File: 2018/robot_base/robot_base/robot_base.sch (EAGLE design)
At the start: 38 parts

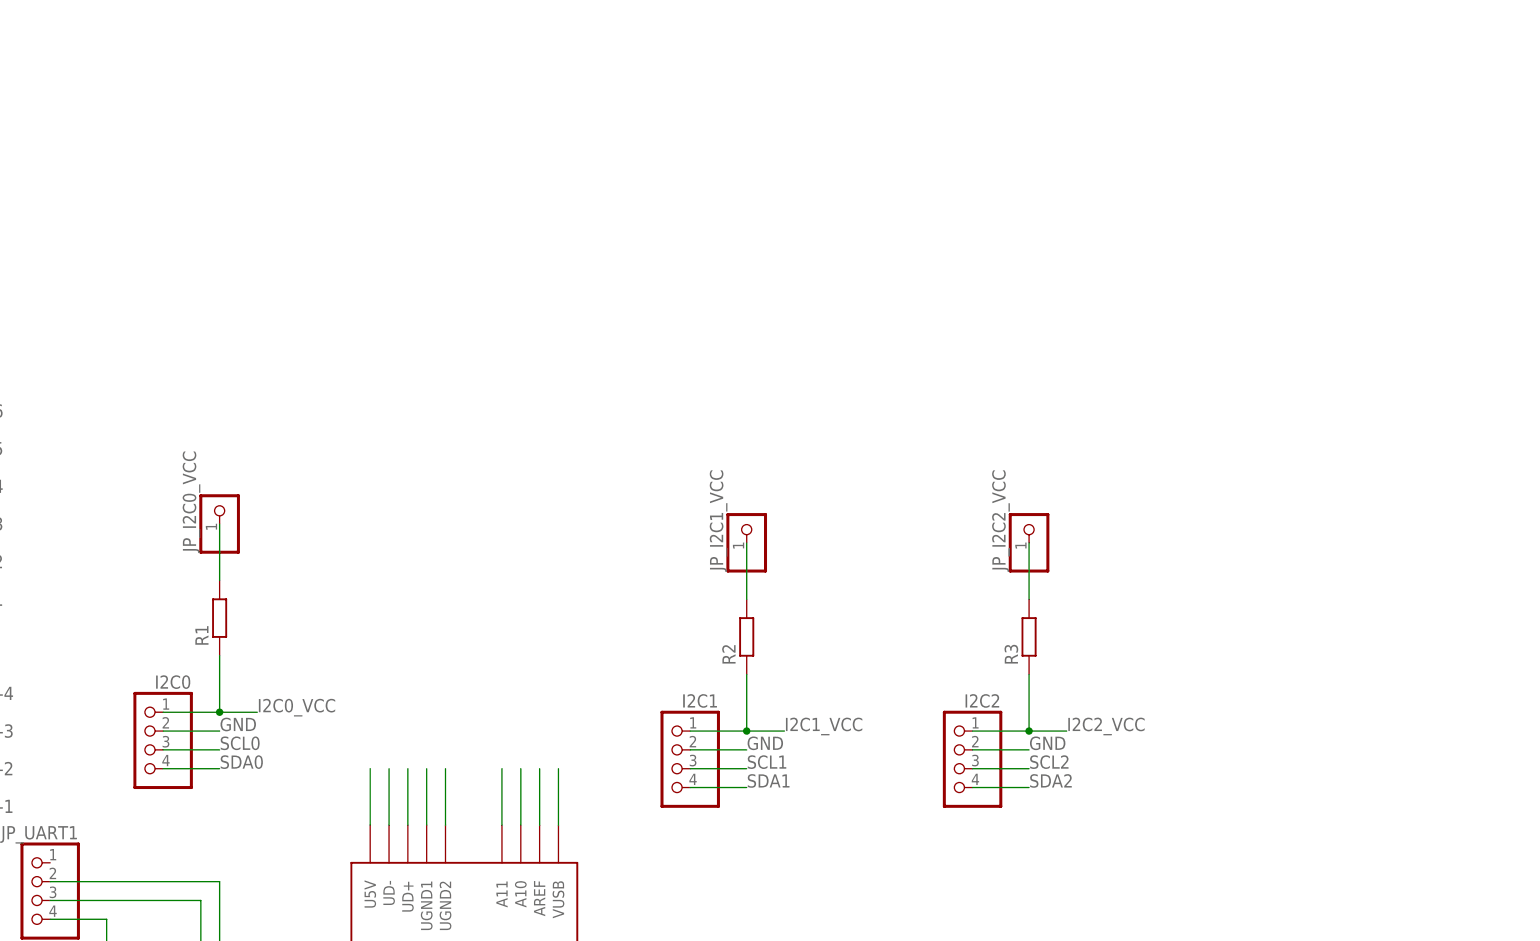
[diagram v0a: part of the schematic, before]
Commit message: Changed I2C Pull-Up resistor selector to match I2C specifications
Note: I2C Resistors doesn't have any value yet. Assessment of line
capacitance is in progress...
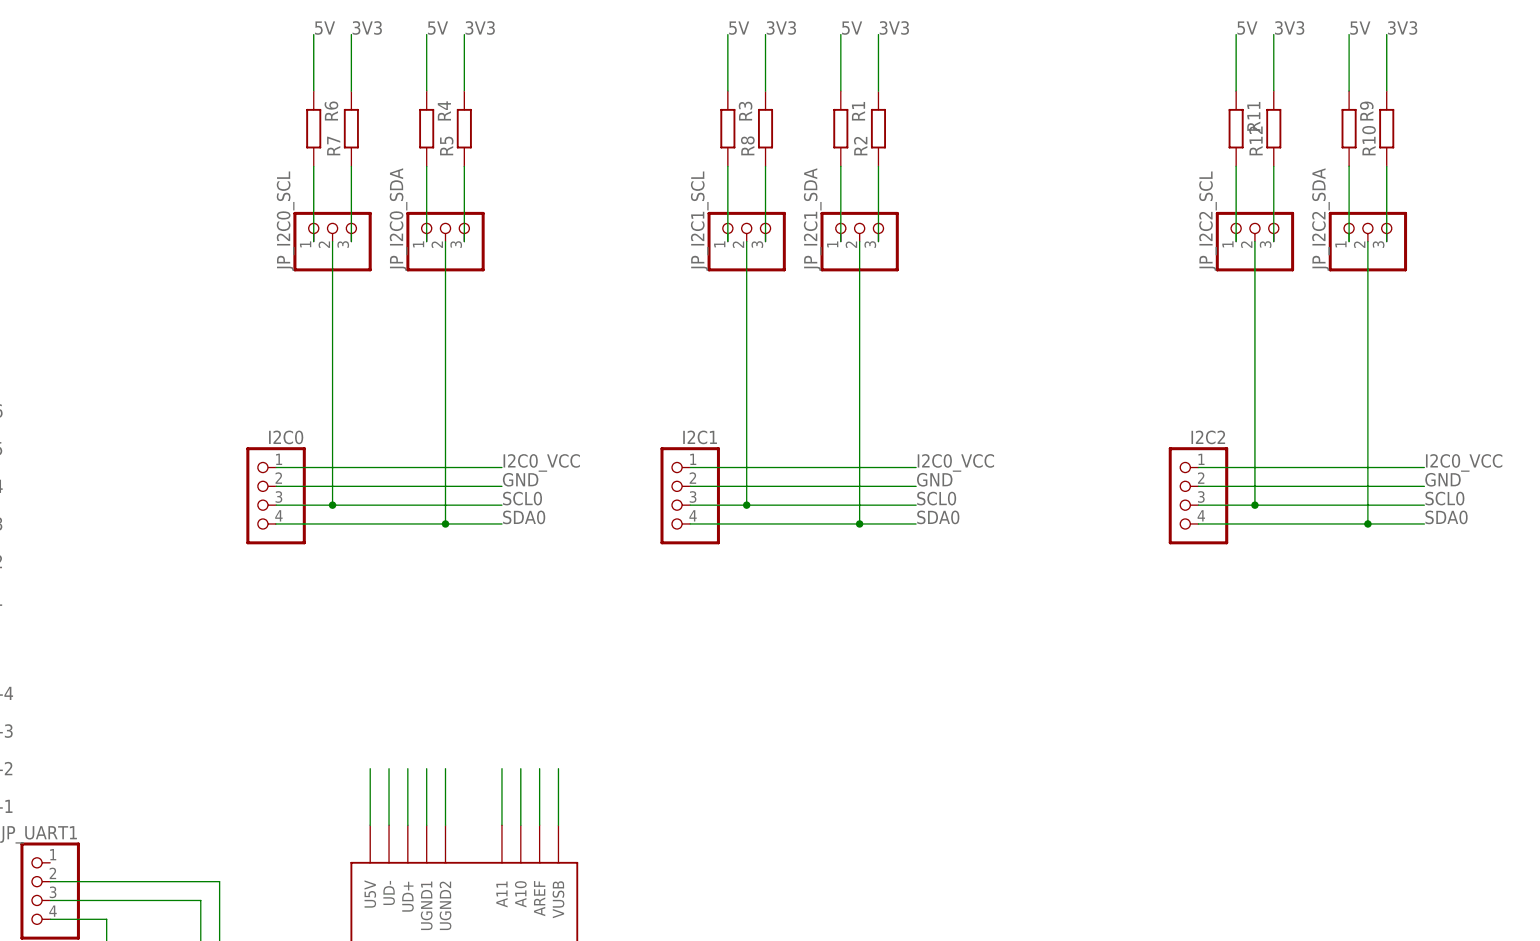
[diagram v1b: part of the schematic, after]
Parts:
- removed JP_I2C0_VCC, JP_I2C1_VCC, JP_I2C2_VCC: (no value), pinhead:PINHD-1X1
- added JP_I2C0_SCL, JP_I2C0_SDA, JP_I2C1_SCL, JP_I2C1_SDA, JP_I2C2_SCL, JP_I2C2_SDA: (no value), pinhead:PINHD-1X3
- added R10, R11, R12, R4, R5, R6, R7, R8, R9: (no value), rcl:R-EU_0204/5
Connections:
- removed net I2C1_VCC: I2C1.1, R2.1
- removed net I2C2_VCC: I2C2.1, R3.1
- new net N$12: JP_I2C0_SDA.1, R4.2
- new net N$13: JP_I2C0_SDA.3, R5.1
- new net N$14: JP_I2C0_SCL.1, R6.2
- new net N$15: JP_I2C0_SCL.3, R7.1
- new net N$16: JP_I2C1_SCL.3, R8.1
- new net N$17: JP_I2C2_SDA.1, R9.2
- new net N$18: JP_I2C2_SDA.3, R10.1
- new net N$19: JP_I2C2_SCL.1, R11.2
- new net N$20: JP_I2C2_SCL.3, R12.1
- net 3V3: now also R10.2, R12.2, R2.2, R5.2, R7.2, R8.2
- net 5V: now also R1.1, R11.1, R3.1, R4.1, R6.1, R9.1
- net I2C0_VCC: now also I2C1.1, I2C2.1; no longer R1.1
- net N$10: now also JP_I2C1_SDA.3, R2.1; no longer JP_I2C1_VCC.1, R2.2
- net N$11: now also JP_I2C1_SCL.1; no longer JP_I2C2_VCC.1
- net N$9: now also JP_I2C1_SDA.1; no longer JP_I2C0_VCC.1
- net SCL0: now also I2C1.3, I2C2.3, JP_I2C0_SCL.2, JP_I2C1_SCL.2, JP_I2C2_SCL.2
- net SCL1: no longer I2C1.3
- net SCL2: no longer I2C2.3
- net SDA0: now also I2C1.4, I2C2.4, JP_I2C0_SDA.2, JP_I2C1_SDA.2, JP_I2C2_SDA.2
- net SDA1: no longer I2C1.4
- net SDA2: no longer I2C2.4
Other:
- moved on the sheet: I2C0, I2C1, I2C2, R1, R2, R3

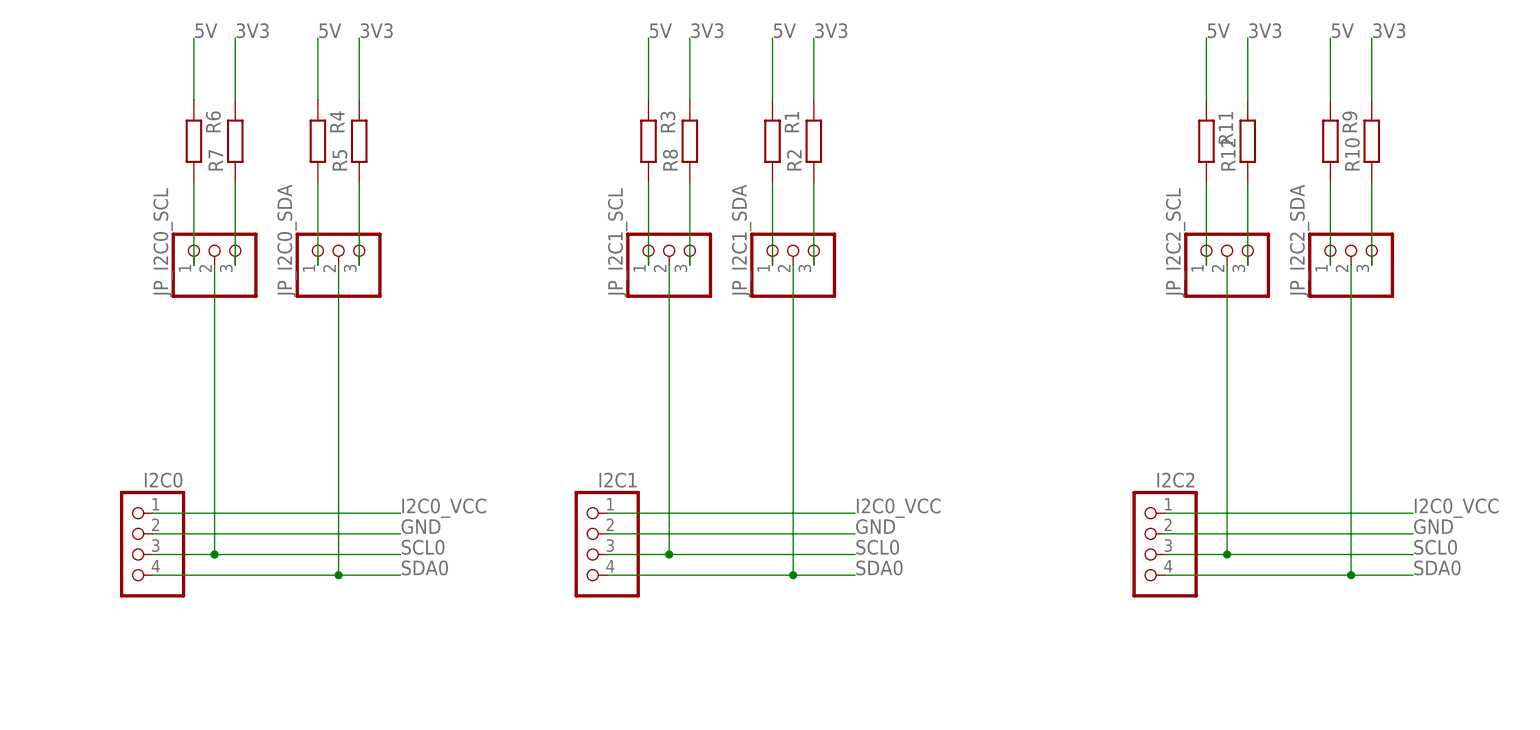
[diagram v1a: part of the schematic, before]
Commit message: Simplified i2c pull-up selector and Partial routing (77%)
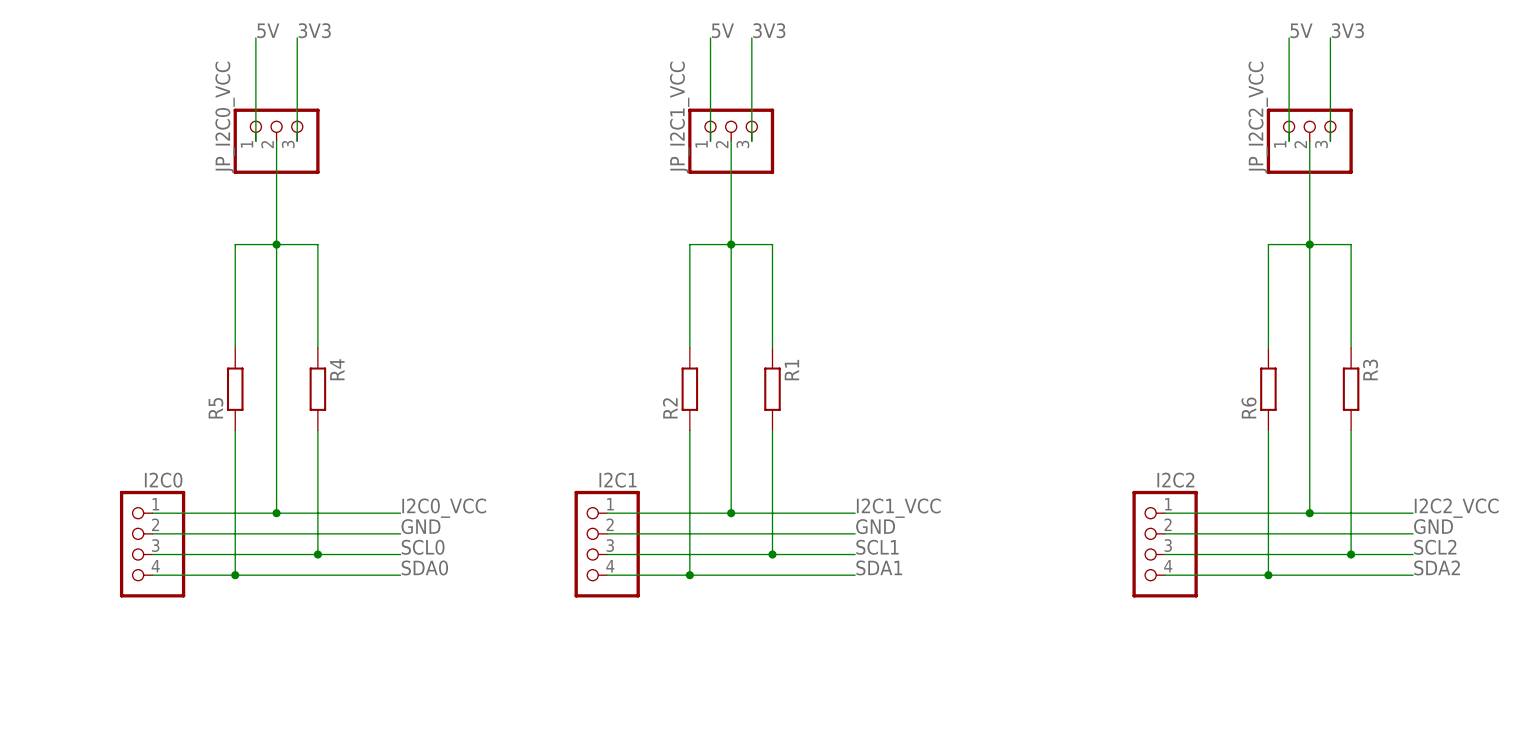
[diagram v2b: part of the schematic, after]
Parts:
- removed JP_I2C0_SCL, JP_I2C0_SDA, JP_I2C1_SCL, JP_I2C1_SDA, JP_I2C2_SCL, JP_I2C2_SDA: (no value), pinhead:PINHD-1X3
- removed R10, R11, R12, R7, R8, R9: (no value), rcl:R-EU_0204/5
- added JP_I2C0_VCC, JP_I2C1_VCC, JP_I2C2_VCC: (no value), pinhead:PINHD-1X3
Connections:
- removed net N$10: JP_I2C1_SDA.3, R2.1
- removed net N$11: JP_I2C1_SCL.1, R3.2
- removed net N$12: JP_I2C0_SDA.1, R4.2
- removed net N$13: JP_I2C0_SDA.3, R5.1
- removed net N$14: JP_I2C0_SCL.1, R6.2
- removed net N$15: JP_I2C0_SCL.3, R7.1
- removed net N$16: JP_I2C1_SCL.3, R8.1
- removed net N$17: JP_I2C2_SDA.1, R9.2
- removed net N$18: JP_I2C2_SDA.3, R10.1
- removed net N$19: JP_I2C2_SCL.1, R11.2
- removed net N$20: JP_I2C2_SCL.3, R12.1
- removed net N$9: JP_I2C1_SDA.1, R1.2
- new net I2C1_VCC: I2C1.1, JP_I2C1_VCC.2, R1.1
- new net I2C2_VCC: I2C2.1, JP_I2C2_VCC.2, R3.1
- net 3V3: now also JP_I2C0_VCC.3, JP_I2C1_VCC.3, JP_I2C2_VCC.3; no longer R10.2, R12.2, R2.2, R5.2, R7.2, R8.2
- net 5V: now also JP_I2C0_VCC.1, JP_I2C1_VCC.1, JP_I2C2_VCC.1; no longer R1.1, R11.1, R3.1, R4.1, R6.1, R9.1
- net I2C0_VCC: now also JP_I2C0_VCC.2, R4.1; no longer I2C1.1, I2C2.1
- net SCL0: now also R4.2; no longer I2C1.3, I2C2.3, JP_I2C0_SCL.2, JP_I2C1_SCL.2, JP_I2C2_SCL.2
- net SCL1: now also I2C1.3, R1.2
- net SCL2: now also I2C2.3, R3.2
- net SDA0: now also R5.1; no longer I2C1.4, I2C2.4, JP_I2C0_SDA.2, JP_I2C1_SDA.2, JP_I2C2_SDA.2
- net SDA1: now also I2C1.4, R2.1
- net SDA2: now also I2C2.4, R6.1
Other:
- moved on the sheet: R1, R2, R3, R4, R5, R6

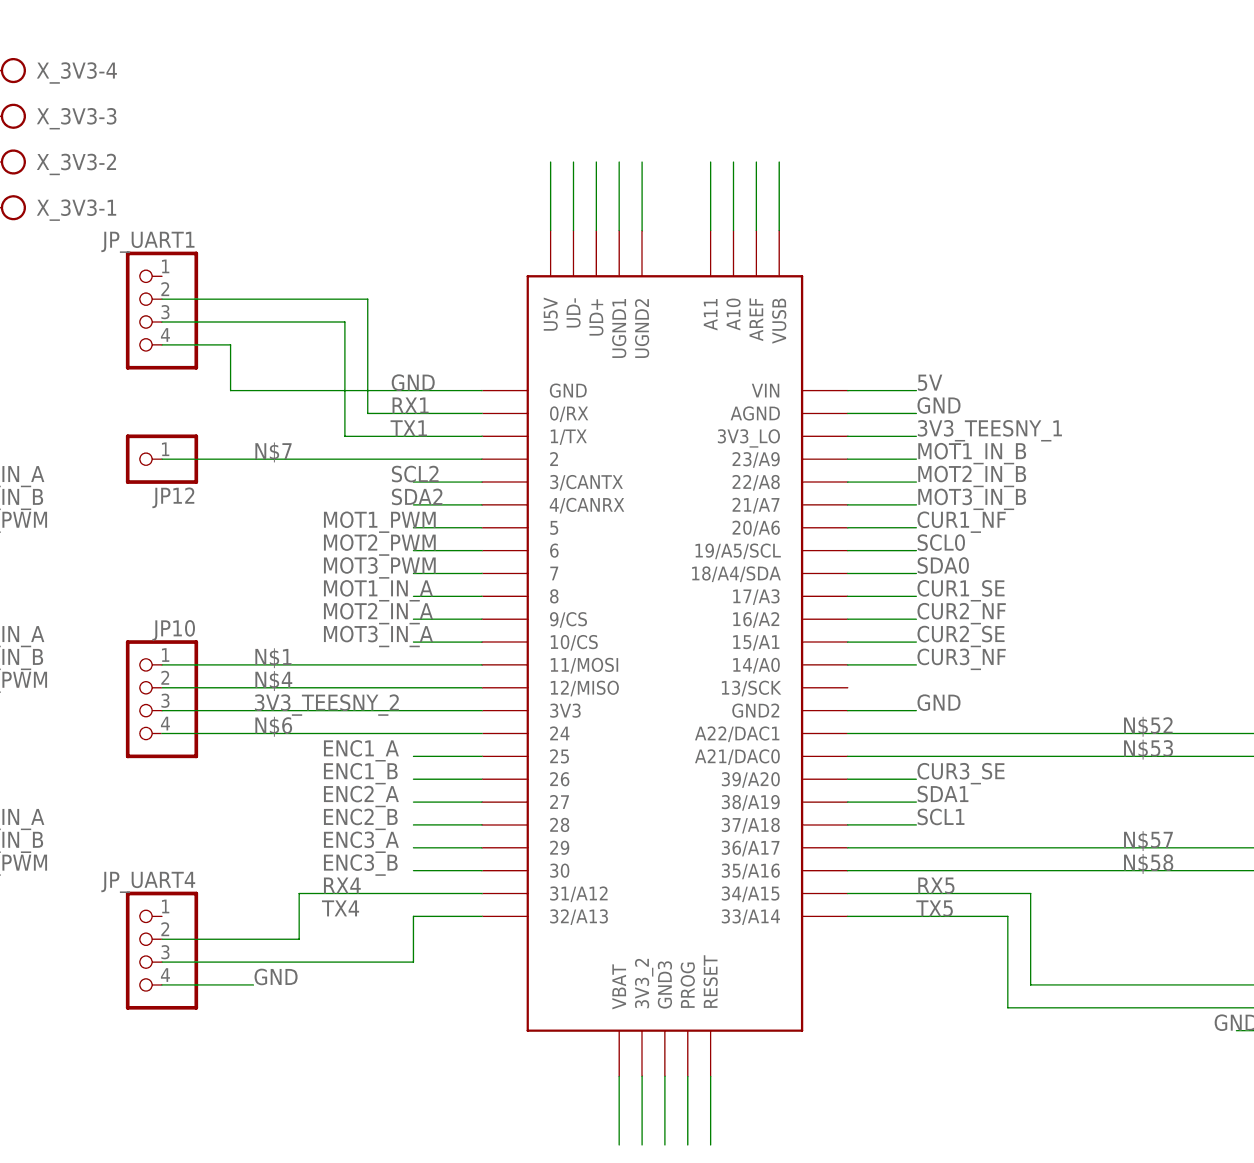
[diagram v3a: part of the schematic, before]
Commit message: robot_base.sch/brd: routing complete, clearance increased and checked. Add teensy package with bigger pads.
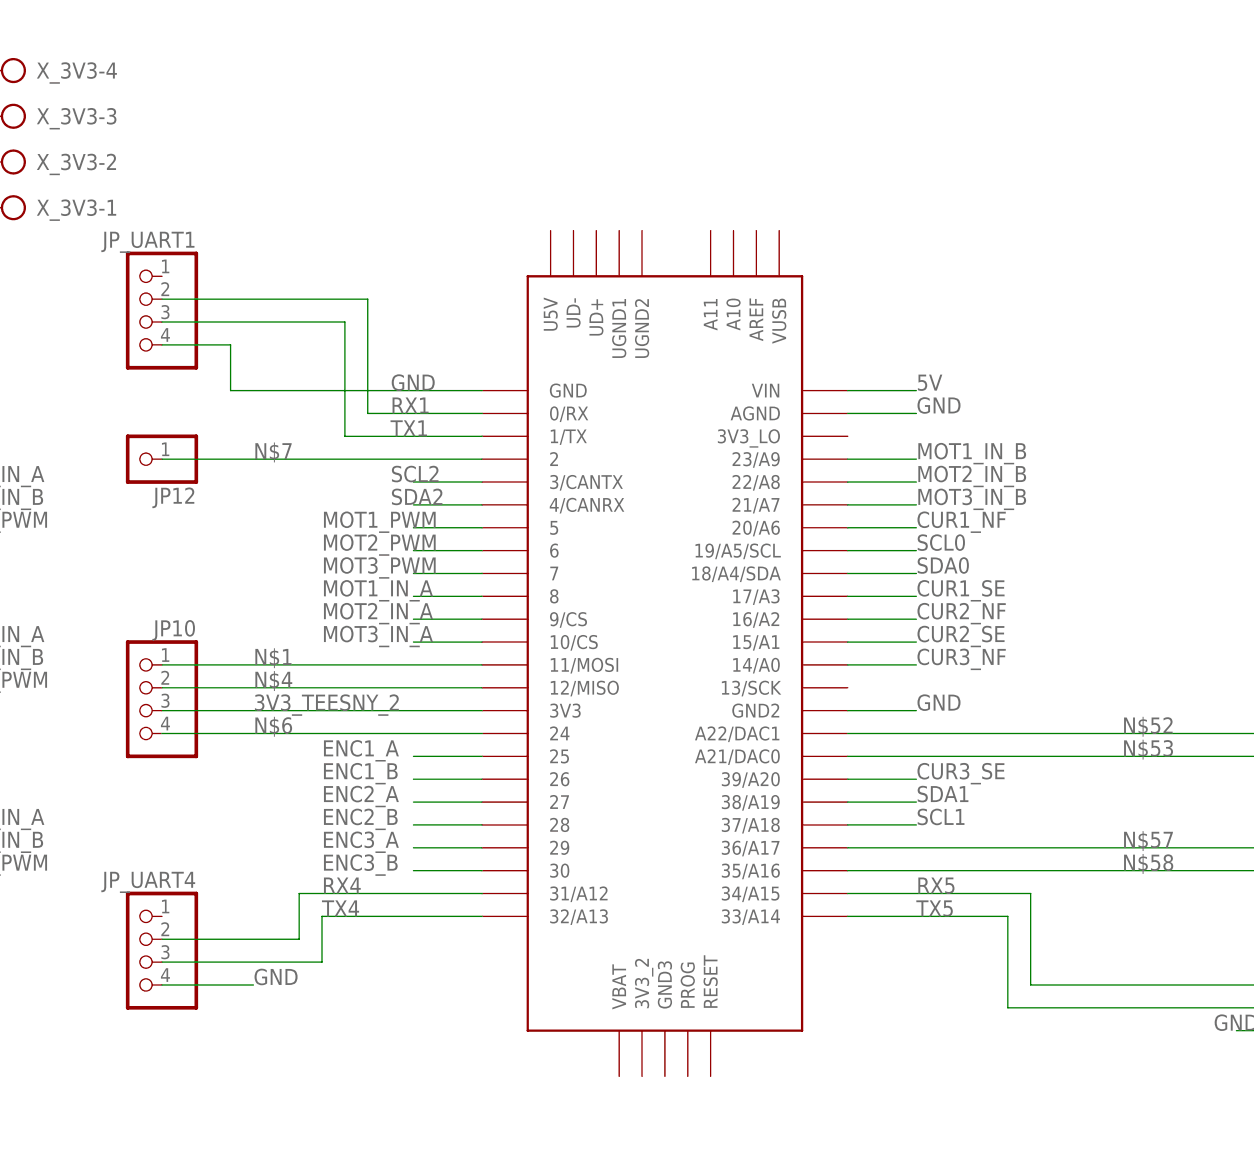
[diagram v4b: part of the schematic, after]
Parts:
- U$1: value TEENSY_3.5/3.6 -> TEENSY_3.5/3.6TEENSY_3.5/3.6_LONG_PADS; device Teensy356:TEENSY_3.5/3.6 -> Teensy356:TEENSY_3.5/3.6TEENSY_3.5/3.6_LONG_PADS
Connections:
- removed net 3V3_TEESNY_1: U$1.3V3_LO
- removed net N$28: U$1.U5V
- removed net N$29: U$1.UD-
- removed net N$30: U$1.UD+
- removed net N$31: U$1.UGND1
- removed net N$32: U$1.UGND2
- removed net N$33: U$1.A11
- removed net N$34: U$1.A10
- removed net N$35: U$1.AREF
- removed net N$36: U$1.VUSB
- removed net N$61: U$1.RESET
- removed net N$62: U$1.PROG
- removed net N$63: U$1.GND3
- removed net N$64: U$1.3V3_2
- removed net N$65: U$1.VBAT
- net I2C0_VCC: now also R5.2
- net I2C1_VCC: now also R2.2
- net I2C2_VCC: now also R6.2
